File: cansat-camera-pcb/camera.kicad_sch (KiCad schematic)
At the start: 18 parts, among them IC2 TLV74315PDBVR, J6 OV5640, U6 TLV74328PDBVR, Y2 ECS-2520MVQ-240-BS-TR

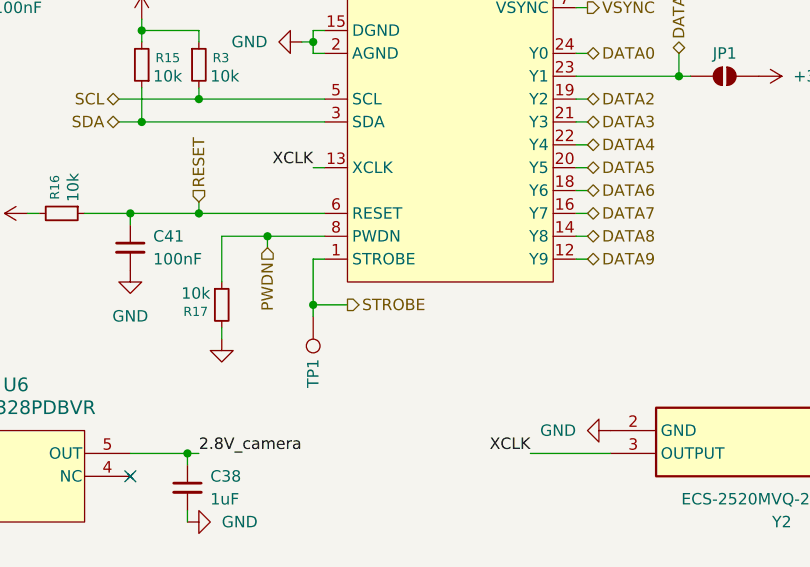
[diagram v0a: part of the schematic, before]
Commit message: adding heatsink+small fixes
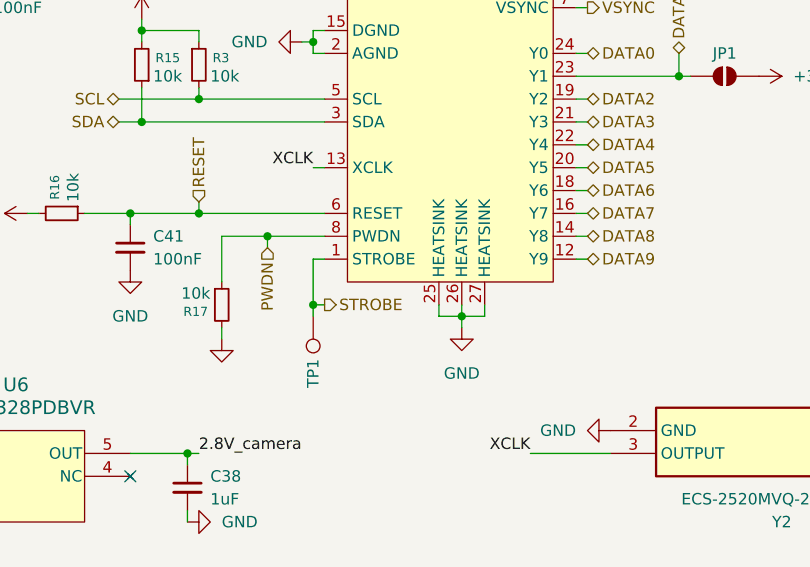
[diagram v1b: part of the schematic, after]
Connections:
- net GND: now also J6.25 (HEATSINK), J6.26 (HEATSINK), J6.27 (HEATSINK)
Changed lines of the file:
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@@
 	)
 	(junction
+		(at 123.19 72.39)
+		(diameter 0)
+		(color 0 0 0 0)
+	)
+	(junction
 		(at 86.36 60.96)
 		(diameter 0)
@@
 	(wire
 		(pts
-			(xy 110.49 71.12) (xy 106.68 71.12)
+			(xy 107.95 71.12) (xy 106.68 71.12)
 		)
 		(stroke
@@
 	(wire
 		(pts
+			(xy 123.19 72.39) (xy 125.73 72.39)
+		)
+		(stroke
+			(width 0)
+			(type default)
+		)
+	)
+	(wire
+		(pts
 			(xy 40.64 125.73) (xy 39.37 125.73)
 		)
@@
 	(wire
 		(pts
+			(xy 120.65 72.39) (xy 123.19 72.39)
+		)
+		(stroke
+			(width 0)
+			(type default)
+		)
+	)
+	(wire
+		(pts
 			(xy 39.37 125.73) (xy 39.37 127)
 		)
@@
 	(wire
 		(pts
+			(xy 123.19 72.39) (xy 123.19 73.66)
+		)
+		(stroke
+			(width 0)
+			(type default)
+		)
+	)
+	(wire
+		(pts
 			(xy 93.98 48.26) (xy 107.95 48.26)
 		)
@@
 	(wire
 		(pts
+			(xy 123.19 71.12) (xy 123.19 72.39)
+		)
+		(stroke
+			(width 0)
+			(type default)
+		)
+	)
+	(wire
+		(pts
 			(xy 85.09 48.26) (xy 93.98 48.26)
 		)
@@
 	(wire
 		(pts
+			(xy 120.65 71.12) (xy 120.65 72.39)
+		)
+		(stroke
+			(width 0)
+			(type default)
+		)
+	)
+	(wire
+		(pts
 			(xy 106.68 66.04) (xy 106.68 71.12)
 		)
@@
 	(wire
 		(pts
+			(xy 125.73 72.39) (xy 125.73 71.12)
+		)
+		(stroke
+			(width 0)
+			(type default)
+		)
+	)
+	(wire
+		(pts
 			(xy 180.34 85.09) (xy 180.34 83.82)
 		)
@@
 	(hierarchical_label "STROBE"
 		(shape output)
-		(at 110.49 71.12 0)
+		(at 107.95 71.12 0)
 		(effects
 			(font
@@
 	)
 	(symbol
+		(lib_id "power:GND")
+		(at 123.19 73.66 0)
+		(unit 1)
+		(exclude_from_sim no)
+		(in_bom yes)
+		(on_board yes)
+		(dnp no)
+		(fields_autoplaced yes)
+		(property "Reference" "#PWR068"
+			(at 123.19 80.01 0)
+			(effects
+				(font
+					(size 1.27 1.27)
+				)
+				(hide yes)
+			)
+		)
+		(property "Value" "GND"
+			(at 123.19 78.74 0)
+			(effects
+				(font
+					(size 1.27 1.27)
+				)
+			)
+		)
+		(property "Footprint" ""
+			(at 123.19 73.66 0)
+			(effects
+				(font
+					(size 1.27 1.27)
+				)
+				(hide yes)
+			)
+		)
+		(property "Datasheet" ""
+			(at 123.19 73.66 0)
+			(effects
+				(font
+					(size 1.27 1.27)
+				)
+				(hide yes)
+			)
+		)
+		(property "Description" "Power symbol creates a global label with name \"GND\" , ground"
+			(at 123.19 73.66 0)
+			(effects
+				(font
+					(size 1.27 1.27)
+				)
+				(hide yes)
+			)
+		)
+		(pin "1"
+		)
+		(instances
+			(project "cansat-camera-pcb"
+				(path "/ff55e53a-9379-43eb-9b08-9bace1f81889/4e5625c8-7acb-416f-9f6b-47ea44535b2e"
+					(reference "#PWR068")
+					(unit 1)
+				)
+			)
+		)
+	)
+	(symbol
 		(lib_id "Device:C_Small")
 		(at 73.66 127 0)
@@
 		(pin "12"
 		)
+		(pin "27"
+		)
+		(pin "26"
+		)
+		(pin "25"
+		)
 		(instances

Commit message: send to production
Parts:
- Y2: footprint ECS2520MVQ240BSTR -> gaia-camera-footprints:ECS2520MVQ240BSTR
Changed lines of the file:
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@@
 			)
 		)
-		(property "Footprint" "ECS2520MVQ240BSTR"
+		(property "Footprint" "gaia-camera-footprints:ECS2520MVQ240BSTR"
 			(at 143.51 -7.29 0)
 			(effects

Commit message: dagobert bácsi hegyekben a steksz
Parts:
- removed Y2: ECS-2520MVQ-240-BS-TR, gaia-camera-footprints:ECS2520MVQ240BSTR, symbol gaia-camera-symbols:ECS-2520MVQ-240-BS-TR

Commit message: milan eszi a havat(unicummal)  (jonas is zabalja)
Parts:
- removed C6: 1uF, Capacitor_SMD:C_0603_1608Metric, symbol Device:C_Small
- removed IC2: TLV74315PDBVR, gaia-camera-footprints:TLV74315PDBVR, symbol gaia-camera-symbols:TLV74315PDBVR
- removed J6: OV5640, gaia-camera-footprints:OV5640, symbol gaia-camera-symbols:OV2640
- removed R15, R16, R17: 10k, Resistor_SMD:R_0402_1005Metric, symbol Device:R_Small
- removed U6: TLV74328PDBVR, gaia-camera-footprints:TLV74328PDBVR, symbol gaia-camera-symbols:TLV74328PDBVR
- added C24, C39: 100nF, Capacitor_SMD:C_0402_1005Metric, symbol Device:C_Small
- added C37: 1uF, Capacitor_SMD:C_0603_1608Metric, symbol Device:C_Small
- added C51: 22pF, Capacitor_SMD:C_0402_1005Metric, symbol Device:C_Small
- added J2: ov5640, gaia-camera-footprints:F33Z1A7Q1E8C24, symbol gaia-camera-symbols:ov5640
- added R6: 10k, Resistor_SMD:R_0402_1005Metric, symbol Device:R_Small
- C38, C44: value 1uF -> 10uF
- C40: value 22pF -> 1uF; footprint Capacitor_SMD:C_0402_1005Metric -> Capacitor_SMD:C_0603_1608Metric
- C41: value 100nF -> 10uF; footprint Capacitor_SMD:C_0402_1005Metric -> Capacitor_SMD:C_0603_1608Metric
- C43: value 100nF -> 1uF; footprint Capacitor_SMD:C_0402_1005Metric -> Capacitor_SMD:C_0603_1608Metric
- C5: value 1uF -> 100nF; footprint Capacitor_SMD:C_0603_1608Metric -> Capacitor_SMD:C_0402_1005Metric
- JP1: value SolderJumper_2_Open -> AF
- TP1: value TestPoint -> Strobe; footprint TestPoint:TestPoint_Pad_2.0x2.0mm -> TestPoint:TestPoint_Pad_1.5x1.5mm
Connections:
- net 1.5V_camera is gone; now on net GND: C42.1, C44.1
- net 2.8V_camera is gone; now on net GND: C38.1, C43.1
- net RESET is gone; now on net GND: C41.1
- net +3.3VA: now also C40.2, C41.2, R3.2, C39.2, J2.11 (DOVDD); no longer C5.2, R3.1
- net GND: now also C40.1, C5.2, C24.1, C37.1, C39.1, C51.2, J2.15 (GND), J2.2 (AGND), J2.25 (MP1), J2.26 (MP2), R6.2; no longer C38.2, C40.2, C41.2, C42.2, C43.2, C44.2, C5.1
- net PCLK: now also C51.1, J2.17 (PCLK); no longer C40.1
- net SCL: now also J2.5 (SCL); no longer R3.2
- net SDA: now also J2.3 (SDA)
- net VSYNC: now also J2.7 (VSYNC)
- net DATA1: no longer names the net of JP1.1 (A)
- net DATA1: now also J2.23 (AF-VCC)
- net STROBE: no longer names the net of TP1.1
- net STROBE: now also J2.1 (STROBE)
- new net CAMERA_1.5V: C42.2, C43.2, C44.2, J2.10 (DVDD)
- new net CAMERA_2.8V: C24.2, C37.2, C38.2, J2.4 (AVDD)
- new net D2: J2.19 (D2)
- new net D3: J2.21 (D3)
- new net D4: J2.22 (D4)
- new net D5: J2.20 (D5)
- new net D6: J2.18 (D6)
- new net D7: J2.16 (D7)
- new net D8: J2.14 (D8)
- new net D9: J2.12 (D9)
- new net HSYNC: J2.9 (HSYNC)
- new net MCLK: J2.13 (MCLK)
- new net pwdnb: J2.8 (PWNDB), R6.1
- new net reset: C5.1, J2.6 (RST), R3.1
- no-connect marks 1 -> 0

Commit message: Finish routing
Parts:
- added JP2: SolderJumper_3_Open, Jumper:SolderJumper-3_P1.3mm_Open_Pad1.0x1.5mm, symbol Jumper:SolderJumper_3_Open
- added Y2: ECS-2520MVQ-240-BS-TR, gaia-camera-footprints:ECS2520MVQ240BSTR, symbol gaia-camera-symbols:ECS-2520MVQ-240-BS-TR
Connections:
- net +3.3VA: now also Y2.1 (TRI-STATE), Y2.4 (VDD)
- net GND: now also Y2.2 (GND)
- net MCLK: now also JP2.3 (B); no longer J2.13 (MCLK)
- new net: JP2.1 (A), Y2.3 (OUTPUT)
- new net XCLK: J2.13 (MCLK), JP2.2 (C)

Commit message: Production v1.3+1.2
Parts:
- added R12, R13, R15, R16, R17, R18, R19, R20, R21, R22, R23, R24: 22, Resistor_SMD:R_0201_0603Metric, symbol Device:R_Small
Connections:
- net D2: now also R16.2; no longer J2.19 (D2)
- net D3: now also R13.2; no longer J2.21 (D3)
- net D4: now also R12.2; no longer J2.22 (D4)
- net D5: now also R15.2; no longer J2.20 (D5)
- net D6: now also R17.2; no longer J2.18 (D6)
- net D7: now also R18.2; no longer J2.16 (D7)
- net D8: now also R19.2; no longer J2.14 (D8)
- net D9: now also R20.2; no longer J2.12 (D9)
- net HSYNC: now also R21.2; no longer J2.9 (HSYNC)
- net MCLK: now also R24.1; no longer JP2.3 (B)
- net PCLK: now also R23.2; no longer C51.1, J2.17 (PCLK)
- net VSYNC: now also R22.2; no longer J2.7 (VSYNC)
- new net: J2.14 (D8), R19.1
- new net: C51.1, J2.17 (PCLK), R23.1
- new net: JP2.3 (B), R24.2
- new net: J2.12 (D9), R20.1
- new net: J2.16 (D7), R18.1
- new net: J2.18 (D6), R17.1
- new net: J2.19 (D2), R16.1
- new net: J2.20 (D5), R15.1
- new net: J2.21 (D3), R13.1
- new net: J2.22 (D4), R12.1
- new net: J2.7 (VSYNC), R22.1
- new net: J2.9 (HSYNC), R21.1
